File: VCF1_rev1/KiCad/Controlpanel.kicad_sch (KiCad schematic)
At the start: 22 parts, among them SW10 SW_SPDT_MSM, SW11 SW_SPDT, SW12 SW_SPDT, SW13 SW_SPDT, SW5 SW_SPDT_MSM, SW6 SW_SPDT_MSM, SW7 SW_SPDT, SW8 SW_SPDT, SW9 SW_SPDT_MSM

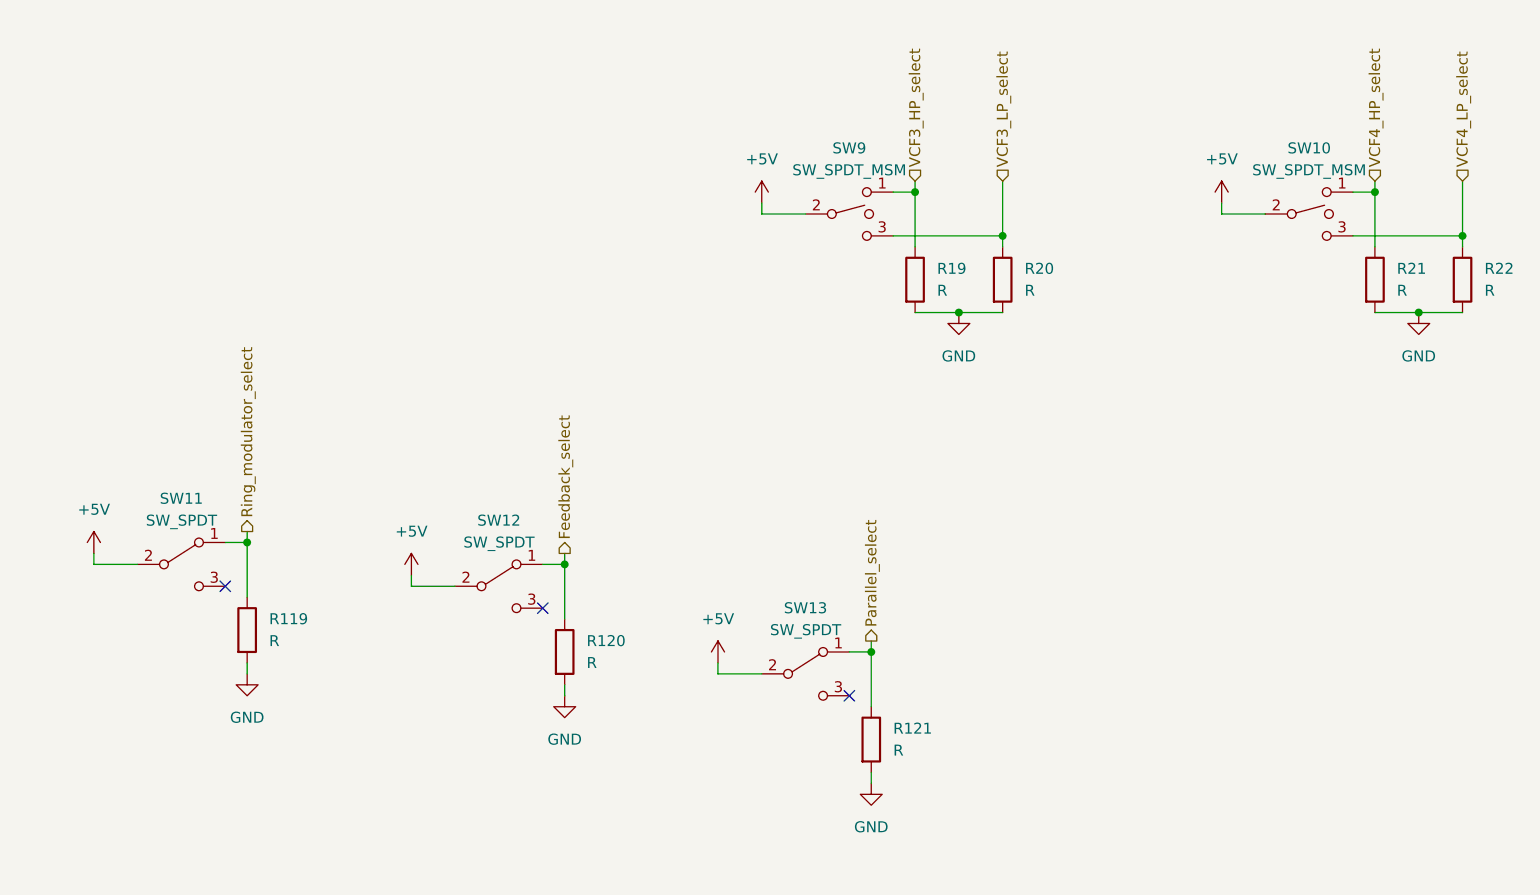
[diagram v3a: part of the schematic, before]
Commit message: Started to populate the PCB and done some small fixes in the schematics.
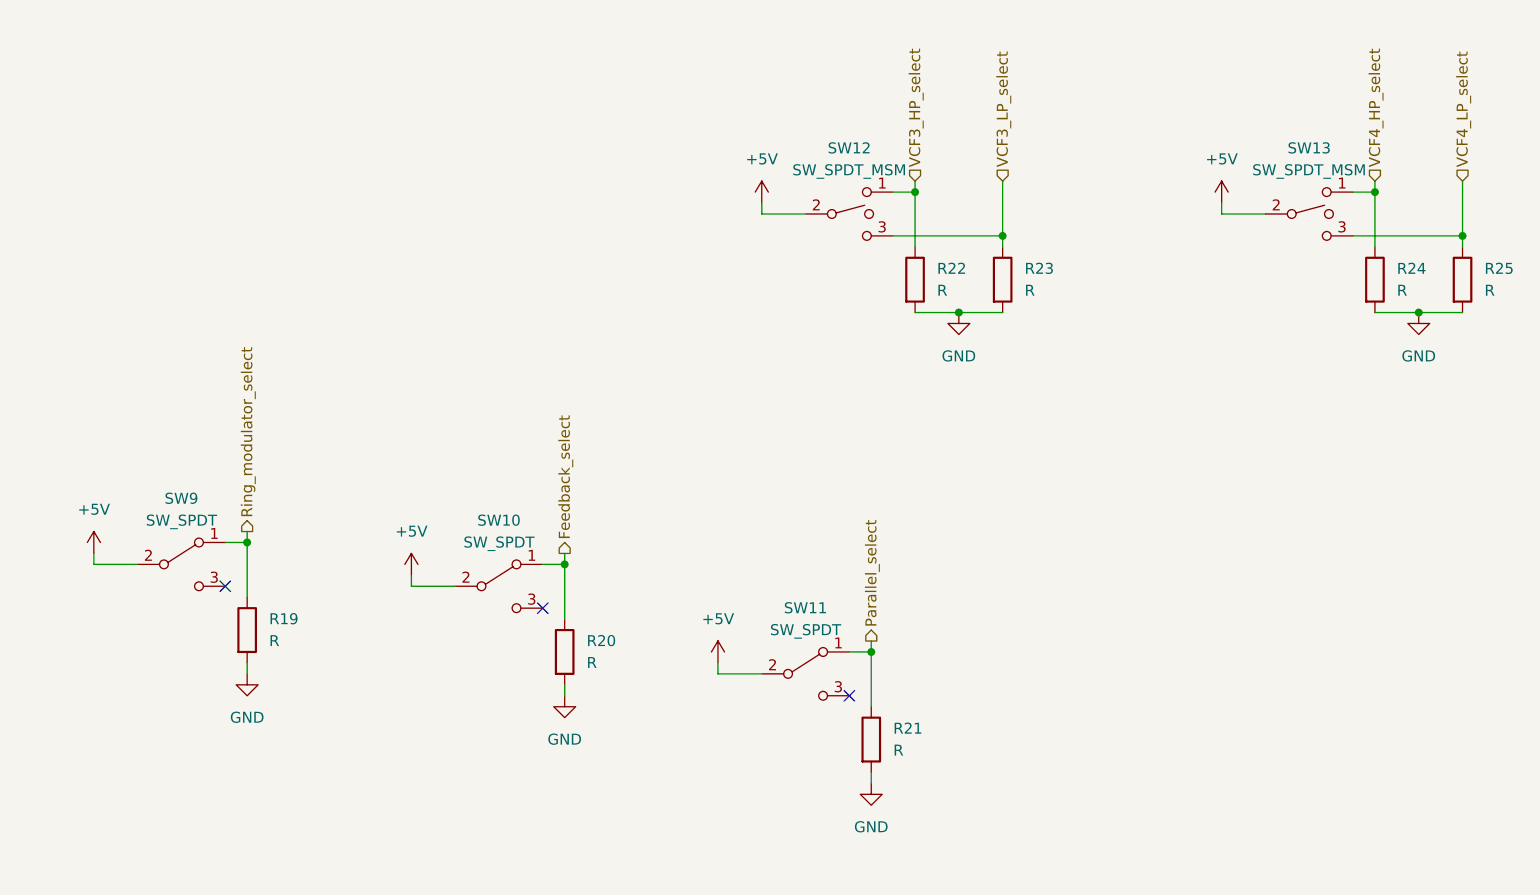
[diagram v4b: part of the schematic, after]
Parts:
- renumbered R119 to R19, R120 to R20, R121 to R21, R19 to R22, R20 to R23, R21 to R24, R22 to R25, SW12 to SW10, SW13 to SW11, SW9 to SW12, SW10 to SW13, SW11 to SW9
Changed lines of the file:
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@@
-(kicad_sch (version 20210621) (generator eeschema)
+(kicad_sch (version 20211123) (generator eeschema)
   (paper "A4")
-  (junction (at 214.63 49.53) (diameter 0) (color 0 0 0 0))
-  (junction (at 168.91 78.74) (diameter 0) (color 0 0 0 0))
-  (junction (at 219.71 40.64) (diameter 0) (color 0 0 0 0))
-  (junction (at 204.47 88.9) (diameter 0) (color 0 0 0 0))
-  (junction (at 82.55 162.56) (diameter 0) (color 0 0 0 0))
-  (junction (at 34.29 137.16) (diameter 0) (color 0 0 0 0))
-  (junction (at 62.23 139.7) (diameter 0) (color 0 0 0 0))
-  (junction (at 132.08 76.2) (diameter 0) (color 0 0 0 0))
-  (junction (at 72.39 148.59) (diameter 0) (color 0 0 0 0))
-  (junction (at 67.31 176.53) (diameter 0) (color 0 0 0 0))
-  (junction (at 262.89 35.56) (diameter 0) (color 0 0 0 0))
-  (junction (at 273.05 40.64) (diameter 0) (color 0 0 0 0))
-  (junction (at 209.55 35.56) (diameter 0) (color 0 0 0 0))
-  (junction (at 52.07 134.62) (diameter 0) (color 0 0 0 0))
-  (junction (at 50.8 39.37) (diameter 0) (color 0 0 0 0))
-  (junction (at 72.39 176.53) (diameter 0) (color 0 0 0 0))
-  (junction (at 62.23 176.53) (diameter 0) (color 0 0 0 0))
-  (junction (at 34.29 151.13) (diameter 0) (color 0 0 0 0))
-  (junction (at 267.97 49.53) (diameter 0) (color 0 0 0 0))
-  (junction (at 55.88 53.34) (diameter 0) (color 0 0 0 0))
-  (junction (at 60.96 44.45) (diameter 0) (color 0 0 0 0))
+  (junction (at 204.47 88.9) (diameter 0) (color 0 0 0 0)
+  )
+  (junction (at 62.23 176.53) (diameter 0) (color 0 0 0 0)
+  )
+  (junction (at 72.39 148.59) (diameter 0) (color 0 0 0 0)
+  )
+  (junction (at 55.88 53.34) (diameter 0) (color 0 0 0 0)
+  )
+  (junction (at 209.55 35.56) (diameter 0) (color 0 0 0 0)
+  )
+  (junction (at 62.23 139.7) (diameter 0) (color 0 0 0 0)
+  )
+  (junction (at 72.39 176.53) (diameter 0) (color 0 0 0 0)
+  )
+  (junction (at 273.05 40.64) (diameter 0) (color 0 0 0 0)
+  )
+  (junction (at 219.71 40.64) (diameter 0) (color 0 0 0 0)
+  )
+  (junction (at 50.8 39.37) (diameter 0) (color 0 0 0 0)
+  )
+  (junction (at 52.07 134.62) (diameter 0) (color 0 0 0 0)
+  )
+  (junction (at 67.31 176.53) (diameter 0) (color 0 0 0 0)
+  )
+  (junction (at 267.97 49.53) (diameter 0) (color 0 0 0 0)
+  )
+  (junction (at 262.89 35.56) (diameter 0) (color 0 0 0 0)
+  )
+  (junction (at 82.55 162.56) (diameter 0) (color 0 0 0 0)
+  )
+  (junction (at 34.29 151.13) (diameter 0) (color 0 0 0 0)
+  )
+  (junction (at 132.08 76.2) (diameter 0) (color 0 0 0 0)
+  )
+  (junction (at 214.63 49.53) (diameter 0) (color 0 0 0 0)
+  )
+  (junction (at 168.91 78.74) (diameter 0) (color 0 0 0 0)
+  )
+  (junction (at 60.96 44.45) (diameter 0) (color 0 0 0 0)
+  )
+  (junction (at 34.29 137.16) (diameter 0) (color 0 0 0 0)
+  )
   (no_connect (at 49.53 153.67))
   (no_connect (at 49.53 167.64))
@@
   (symbol (lib_id "power:+5V") (at 151.13 80.01 0) (unit 1)
     (in_bom yes) (on_board yes) (fields_autoplaced)
-    (property "Reference" "#PWR083" (id 0) (at 151.13 83.82 0)
+    (property "Reference" "#PWR012" (id 0) (at 151.13 83.82 0)
       (effects (font (size 1.27 1.27)) hide)
     )
@@
   (symbol (lib_id "Switch:SW_SPDT") (at 161.29 81.28 0) (unit 1)
     (in_bom yes) (on_board yes) (fields_autoplaced)
-    (property "Reference" "SW12" (id 0) (at 161.29 73.66 0))
+    (property "Reference" "SW10" (id 0) (at 161.29 73.66 0))
     (property "Value" "SW_SPDT" (id 1) (at 161.29 76.2 0))
     (property "Footprint" "" (id 2) (at 161.29 81.28 0)
@@
   (symbol (lib_id "power:GND") (at 204.47 104.14 0) (unit 1)
     (in_bom yes) (on_board yes) (fields_autoplaced)
-    (property "Reference" "#PWR086" (id 0) (at 204.47 110.49 0)
+    (property "Reference" "#PWR016" (id 0) (at 204.47 110.49 0)
       (effects (font (size 1.27 1.27)) hide)
     )
@@
   (symbol (lib_id "Device:R") (at 219.71 45.72 0) (unit 1)
     (in_bom yes) (on_board yes) (fields_autoplaced)
-    (property "Reference" "R20" (id 0) (at 222.25 44.4499 0)
+    (property "Reference" "R23" (id 0) (at 222.25 44.4499 0)
       (effects (font (size 1.27 1.27)) (justify left))
     )
@@
   (symbol (lib_id "power:+5V") (at 186.69 90.17 0) (unit 1)
     (in_bom yes) (on_board yes) (fields_autoplaced)
-    (property "Reference" "#PWR085" (id 0) (at 186.69 93.98 0)
+    (property "Reference" "#PWR014" (id 0) (at 186.69 93.98 0)
       (effects (font (size 1.27 1.27)) hide)
     )
@@
   (symbol (lib_id "power:+5V") (at 114.3 77.47 0) (unit 1)
     (in_bom yes) (on_board yes) (fields_autoplaced)
-    (property "Reference" "#PWR081" (id 0) (at 114.3 81.28 0)
+    (property "Reference" "#PWR010" (id 0) (at 114.3 81.28 0)
       (effects (font (size 1.27 1.27)) hide)
     )
@@
   (symbol (lib_id "Device:R") (at 209.55 45.72 0) (unit 1)
     (in_bom yes) (on_board yes) (fields_autoplaced)
-    (property "Reference" "R19" (id 0) (at 212.09 44.4499 0)
+    (property "Reference" "R22" (id 0) (at 212.09 44.4499 0)
       (effects (font (size 1.27 1.27)) (justify left))
     )
@@
   (symbol (lib_id "power:+5V") (at 191.77 36.83 0) (unit 1)
     (in_bom yes) (on_board yes) (fields_autoplaced)
-    (property "Reference" "#PWR010" (id 0) (at 191.77 40.64 0)
+    (property "Reference" "#PWR015" (id 0) (at 191.77 40.64 0)
       (effects (font (size 1.27 1.27)) hide)
     )
@@
   (symbol (lib_id "Device:R") (at 132.08 86.36 0) (unit 1)
     (in_bom yes) (on_board yes) (fields_autoplaced)
-    (property "Reference" "R119" (id 0) (at 134.62 85.0899 0)
+    (property "Reference" "R19" (id 0) (at 134.62 85.0899 0)
       (effects (font (size 1.27 1.27)) (justify left))
     )
@@
   (symbol (lib_id "Device:R") (at 262.89 45.72 0) (unit 1)
     (in_bom yes) (on_board yes) (fields_autoplaced)
-    (property "Reference" "R21" (id 0) (at 265.43 44.4499 0)
+    (property "Reference" "R24" (id 0) (at 265.43 44.4499 0)
       (effects (font (size 1.27 1.27)) (justify left))
     )
@@
   (symbol (lib_id "Device:R") (at 168.91 88.9 0) (unit 1)
     (in_bom yes) (on_board yes) (fields_autoplaced)
-    (property "Reference" "R120" (id 0) (at 171.45 87.6299 0)
+    (property "Reference" "R20" (id 0) (at 171.45 87.6299 0)
       (effects (font (size 1.27 1.27)) (justify left))
     )
@@
   (symbol (lib_id "Switch:SW_SPDT") (at 196.85 91.44 0) (unit 1)
     (in_bom yes) (on_board yes) (fields_autoplaced)
-    (property "Reference" "SW13" (id 0) (at 196.85 83.82 0))
+    (property "Reference" "SW11" (id 0) (at 196.85 83.82 0))
     (property "Value" "SW_SPDT" (id 1) (at 196.85 86.36 0))
     (property "Footprint" "" (id 2) (at 196.85 91.44 0)
@@
   (symbol (lib_id "Device:R") (at 204.47 99.06 0) (unit 1)
     (in_bom yes) (on_board yes) (fields_autoplaced)
-    (property "Reference" "R121" (id 0) (at 207.01 97.7899 0)
+    (property "Reference" "R21" (id 0) (at 207.01 97.7899 0)
       (effects (font (size 1.27 1.27)) (justify left))
     )
@@
   (symbol (lib_id "Switch:SW_SPDT") (at 124.46 78.74 0) (unit 1)
     (in_bom yes) (on_board yes) (fields_autoplaced)
-    (property "Reference" "SW11" (id 0) (at 124.46 71.12 0))
+    (property "Reference" "SW9" (id 0) (at 124.46 71.12 0))
     (property "Value" "SW_SPDT" (id 1) (at 124.46 73.66 0))
     (property "Footprint" "" (id 2) (at 124.46 78.74 0)
@@
   (symbol (lib_id "power:GND") (at 267.97 49.53 0) (unit 1)
     (in_bom yes) (on_board yes) (fields_autoplaced)
-    (property "Reference" "#PWR013" (id 0) (at 267.97 55.88 0)
+    (property "Reference" "#PWR019" (id 0) (at 267.97 55.88 0)
       (effects (font (size 1.27 1.27)) hide)
     )
@@
   (symbol (lib_id "power:+5V") (at 245.11 36.83 0) (unit 1)
     (in_bom yes) (on_board yes) (fields_autoplaced)
-    (property "Reference" "#PWR012" (id 0) (at 245.11 40.64 0)
+    (property "Reference" "#PWR018" (id 0) (at 245.11 40.64 0)
       (effects (font (size 1.27 1.27)) hide)
     )
@@
   (symbol (lib_id "power:GND") (at 214.63 49.53 0) (unit 1)
     (in_bom yes) (on_board yes) (fields_autoplaced)
-    (property "Reference" "#PWR011" (id 0) (at 214.63 55.88 0)
+    (property "Reference" "#PWR017" (id 0) (at 214.63 55.88 0)
       (effects (font (size 1.27 1.27)) hide)
     )
@@
   (symbol (lib_id "Device:R") (at 273.05 45.72 0) (unit 1)
     (in_bom yes) (on_board yes) (fields_autoplaced)
-    (property "Reference" "R22" (id 0) (at 275.59 44.4499 0)
+    (property "Reference" "R25" (id 0) (at 275.59 44.4499 0)
       (effects (font (size 1.27 1.27)) (justify left))
     )
@@
   (symbol (lib_id "Switch:SW_SPDT_MSM") (at 201.93 38.1 0) (unit 1)
     (in_bom yes) (on_board yes) (fields_autoplaced)
-    (property "Reference" "SW9" (id 0) (at 201.93 30.48 0))
+    (property "Reference" "SW12" (id 0) (at 201.93 30.48 0))
     (property "Value" "SW_SPDT_MSM" (id 1) (at 201.93 33.02 0))
     (property "Footprint" "" (id 2) (at 201.93 38.1 0)
@@
   (symbol (lib_id "power:GND") (at 168.91 93.98 0) (unit 1)
     (in_bom yes) (on_board yes) (fields_autoplaced)
-    (property "Reference" "#PWR084" (id 0) (at 168.91 100.33 0)
+    (property "Reference" "#PWR013" (id 0) (at 168.91 100.33 0)
       (effects (font (size 1.27 1.27)) hide)
     )
@@
   (symbol (lib_id "power:GND") (at 132.08 91.44 0) (unit 1)
     (in_bom yes) (on_board yes) (fields_autoplaced)
-    (property "Reference" "#PWR082" (id 0) (at 132.08 97.79 0)
+    (property "Reference" "#PWR011" (id 0) (at 132.08 97.79 0)
       (effects (font (size 1.27 1.27)) hide)
     )
@@
   (symbol (lib_id "Switch:SW_SPDT_MSM") (at 255.27 38.1 0) (unit 1)
     (in_bom yes) (on_board yes) (fields_autoplaced)
-    (property "Reference" "SW10" (id 0) (at 255.27 30.48 0))
+    (property "Reference" "SW13" (id 0) (at 255.27 30.48 0))
     (property "Value" "SW_SPDT_MSM" (id 1) (at 255.27 33.02 0))
     (property "Footprint" "" (id 2) (at 255.27 38.1 0)
